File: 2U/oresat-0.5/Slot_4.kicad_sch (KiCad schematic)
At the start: 4 parts

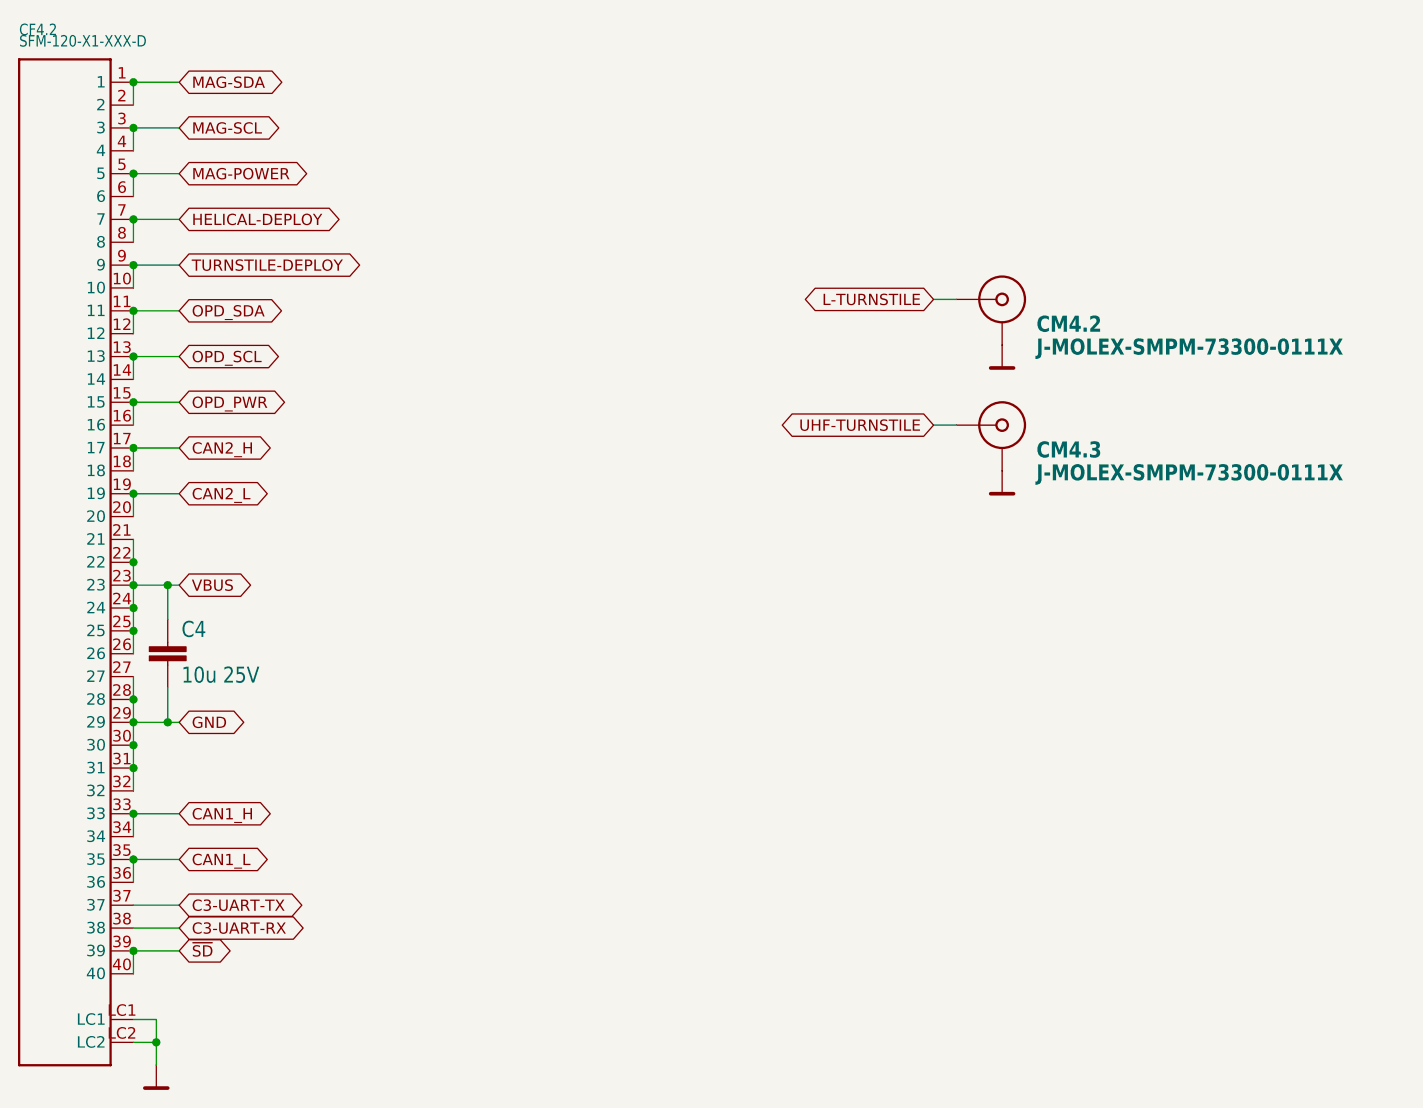
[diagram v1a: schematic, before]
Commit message: Fixed all (most) of the issues from Eagle imports
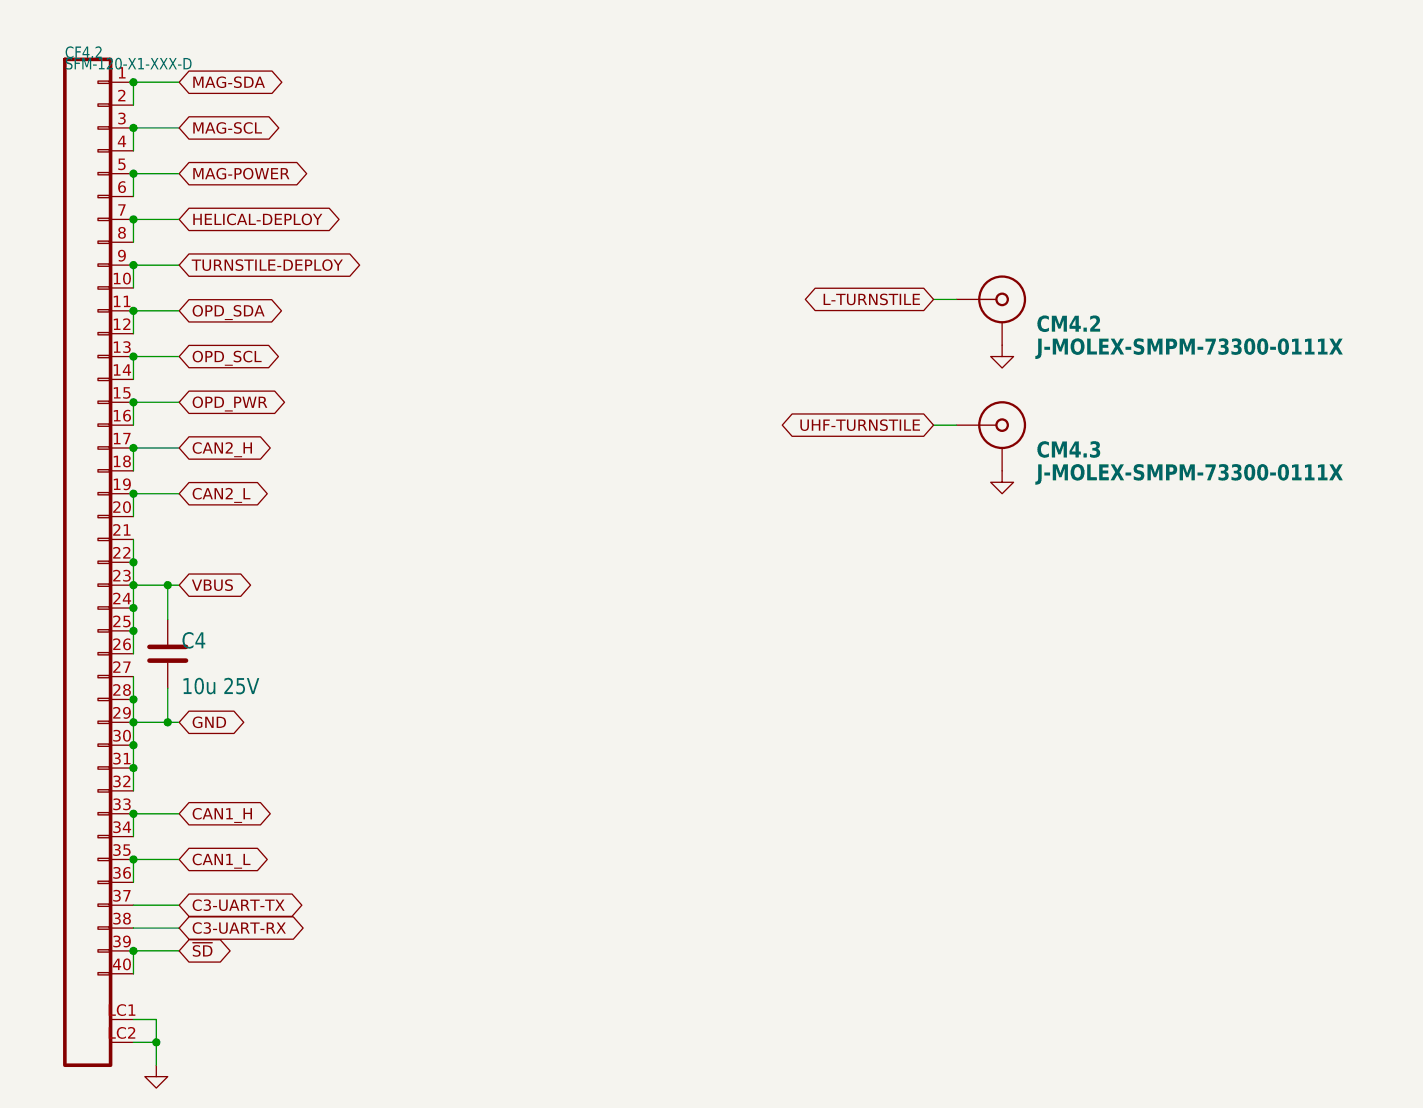
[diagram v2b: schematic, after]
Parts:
- C4: symbol oresat0-1u-backplane-eagle-import:C-EU1206-B -> Device:C
- CF4.2: symbol oresat-backplane-2u-eagle-import:SFM-120-X1-XXX-D -> oresat-connectors:J-SAMTEC-TFM-120-01-L-D-RA
- CM4.2, CM4.3: symbol oresat-symbols:J-MOLEX-SMPM-73300-0111X_1 -> oresat-connectors:J-MOLEX-SMPM-73300-0111X_1

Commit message: Moved entire schematic to single page
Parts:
- removed C4: 10u 25V, Capacitor_SMD:C_1206_3216Metric, symbol Device:C
- removed CF4.2: SFM-120-X1-XXX-D, oresat-connectors:J-SAMTEC-SFM-120-X1-XXX-D, symbol oresat-connectors:J-SAMTEC-TFM-120-01-L-D-RA
- removed CM4.2, CM4.3: J-MOLEX-SMPM-73300-0111X, oresat-connectors:J-MOLEX-SMPM-73300-0111X-long, symbol oresat-connectors:J-MOLEX-SMPM-73300-0111X_1
